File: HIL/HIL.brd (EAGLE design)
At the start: 129.5 x 103.9 mm, 269 parts, among them J1 JTAG_ARM_10PIN, J4 JTAG_ARM_10PIN, M0S0 TPB1,27, M0S1 TPB1,27, M0S2 TPB1,27, M0S3 TPB1,27, M1S0 M0S3, M1S1 M0S3, M1S2 M0S3, M1S3 M0S3, M2S0 M0S3, M2S1 M0S3, M2S2 M0S3, M2S3 M0S3, U1 CD74HC4067SM96, U10 INA219AIDCNR, U11 INA219AIDCNR, U12 INA219AIDCNR, U13 TM4C1294NCPDT, U14 ADUM1201ARZ, U15 SN65HVD230D, U16 TL1963AKTTR., U17 FT230XS, U2 TL1963AKTTR., U3 CD74HC4067SM96, U4 CD74HC4067SM96, U5 MCP4725A0T-E/CH, U6 TL1963AKTTR., U7 MCP2003-E/SN, U9 INA219AIDCNR, X1 A1944-50, X2 A1944-50, X4 A1944-50, Y3 NX3225GA

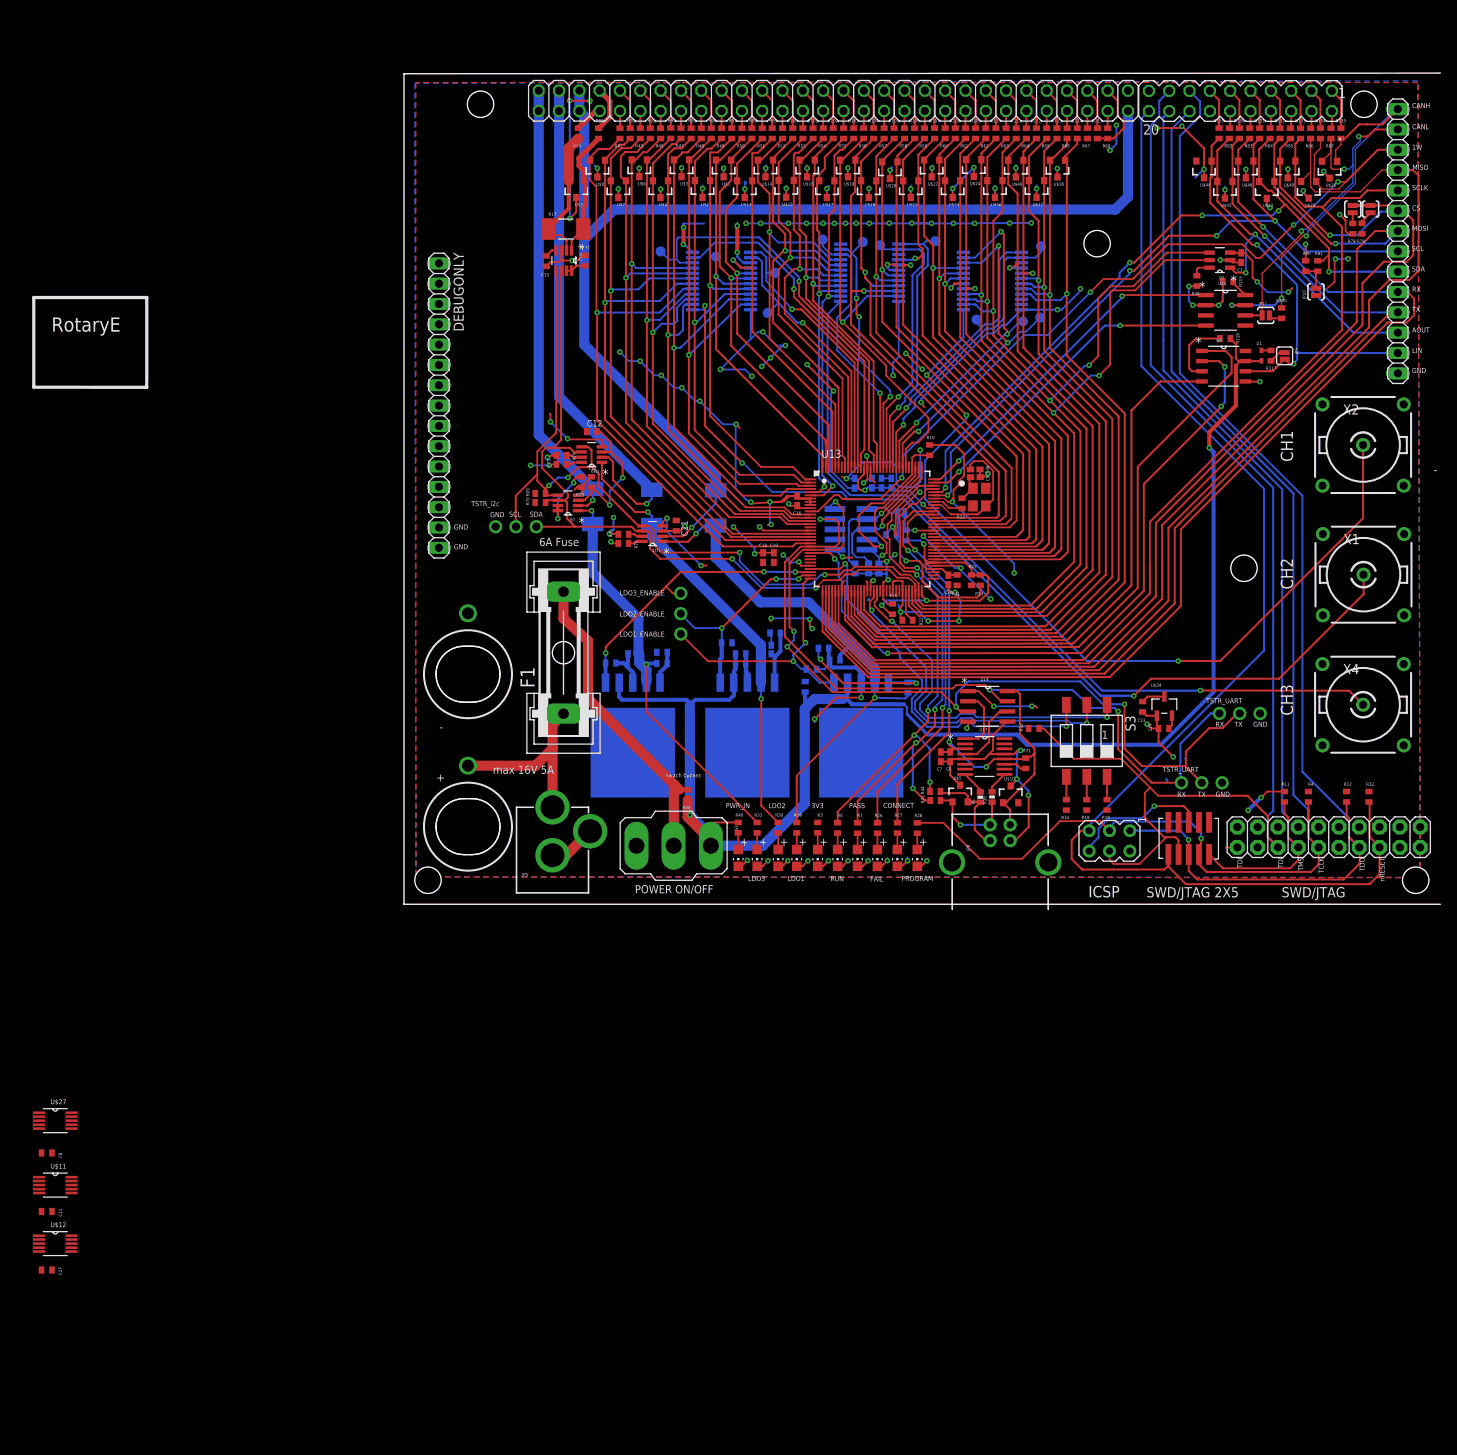
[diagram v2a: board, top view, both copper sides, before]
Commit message: Remove: 1 chanel DAC Add: 8 CH DAC Update: libraries
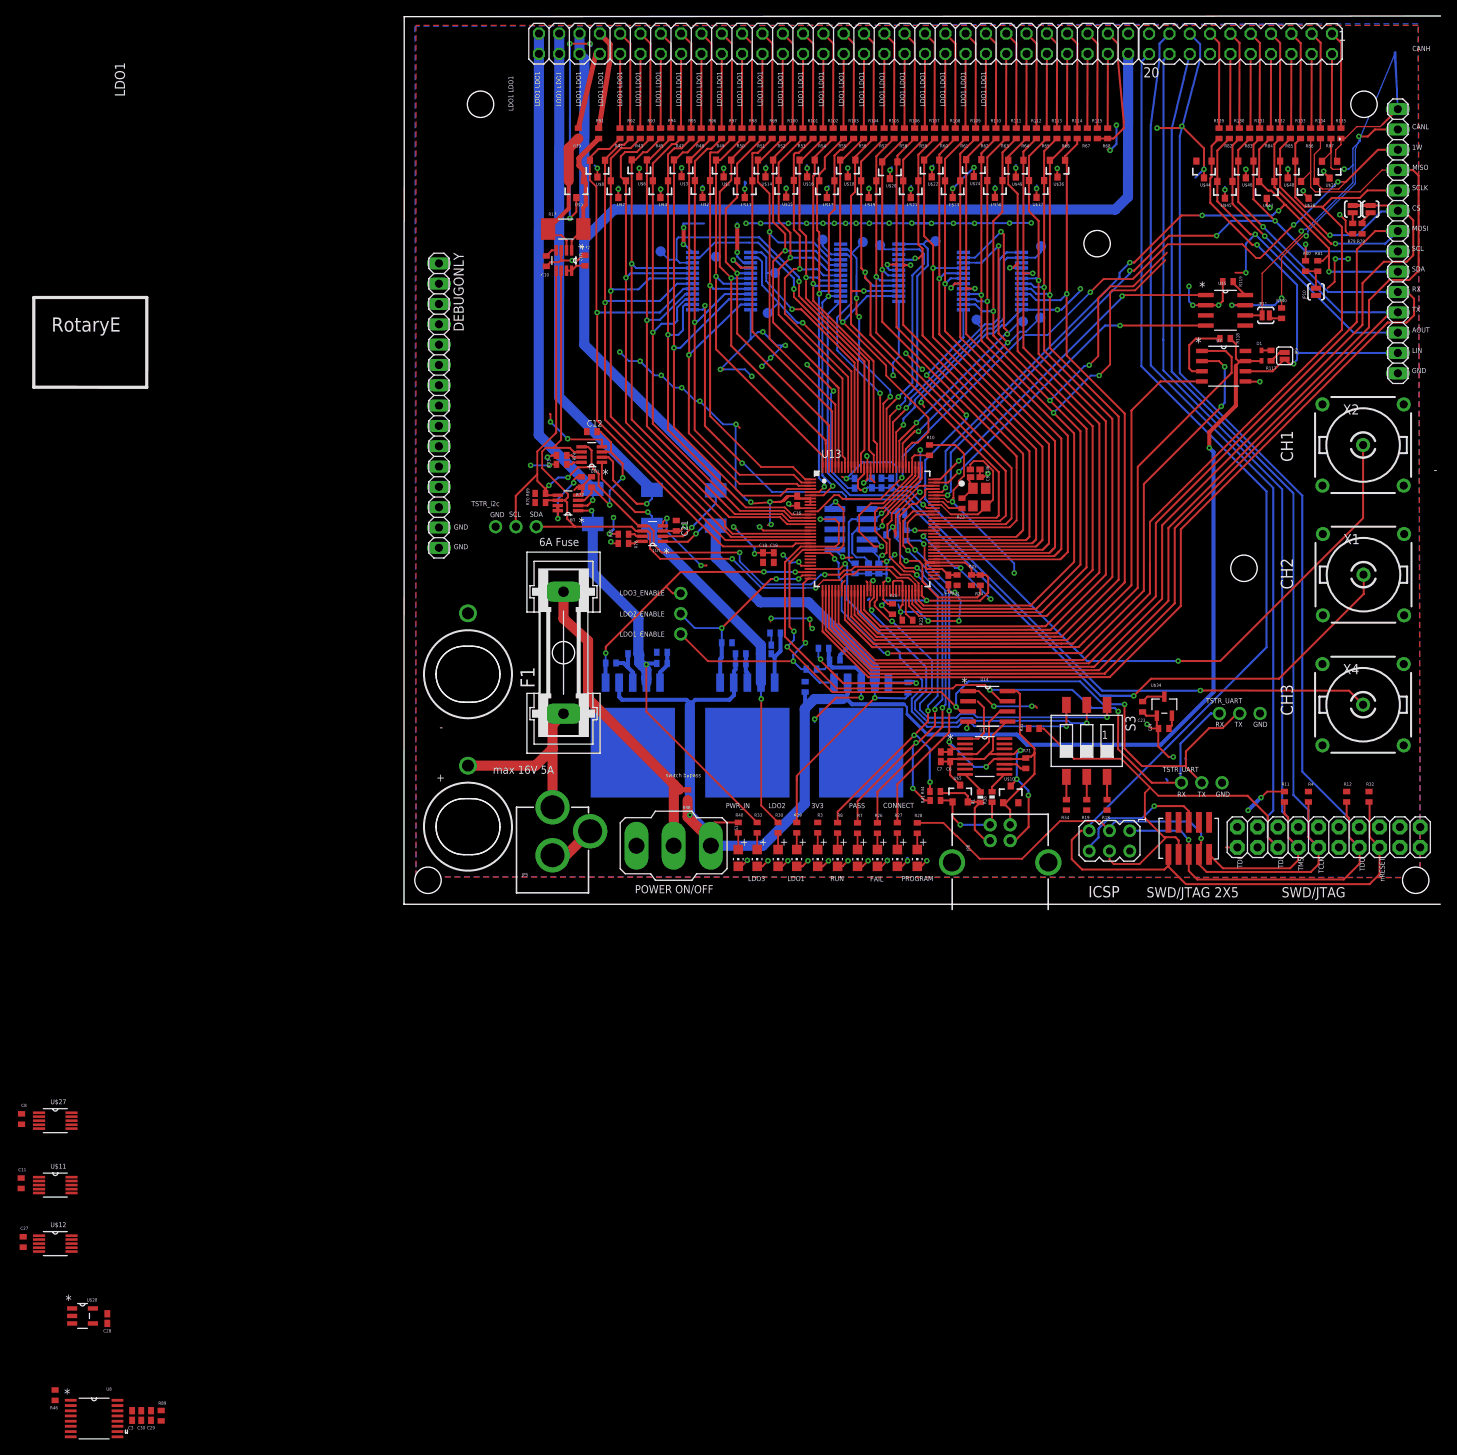
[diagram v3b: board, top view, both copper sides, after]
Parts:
- removed U5: MCP4725A0T-E/CH, MCP4725:SOT95P270X145-6N
- added C28: 0.1uF, rcl:C0402K
- added C29: 1uF, rcl:C0402K
- added C30: 10uF, rcl:C0402K
- added R89: 4k7, resistor:R0402
- added U$28: 24AA04T-I/OT, microchip_E14:SOT95P290X145-5N
- added U8: DAC7578SPW, Texas Instruments_E14:SOP65P640X120-16N
- R46: value 4.7k -> 4k7
- moved C3 200.4 mm to (-34.0, -63.9)
- moved R46 199.4 mm to (-43.6, -61.4)
- moved JP6 7.14 mm to (55.0, 107.6)
- moved SV1 7.14 mm to (104.6, 107.5)
- moved C8 5.28 mm to (-47.8, -26.8), turned to 90 degrees
- moved C11 4.77 mm to (-47.9, -34.9), turned to 90 degrees
- moved C27 4.58 mm to (-47.6, -42.2), turned to 90 degrees
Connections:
- net ADJ3 renamed LDO1_ADJ
- net ADJ4 renamed LDO2_ADJ
- net ADJ5 renamed LDO3_ADJ
- net N$40 renamed VIN
- removed net N$216: C23.1, U$34.3
- new net AOUT_1: U8.4
- new net AOUT_2: U8.13
- new net AOUT_3: U8.5
- new net AOUT_4: U8.12
- new net AOUT_5: U8.6
- new net AOUT_6: U8.11
- new net AOUT_7: U8.7
- new net AOUT_8: U8.10
- new net N$40: C29.2, C3.2, C30.2, R46.1, R89.2, U8.3, U8.8
- new net N$81: R89.1, U8.9
- net DUT_AOUT1: no longer U5.1
- net GND: now also C28.1, C29.1, C3.1, C30.1, U$28.2, U$28.5, U8.14; no longer C3.2, R46.2, U5.2
- net HOST_UART_TX: now also U14.7; no longer U14.2
- net N$1: now also R46.2, U8.1; no longer R46.1, U5.6
- net POWER_IN_12V: now also C23.1, U$34.3
- net TSTR_3V3: now also C28.2, U$28.4; no longer C3.1, U5.3
- net TSTR_RX: now also U14.2; no longer U14.7
- net TSTR_SCL: now also U$28.1, U8.16; no longer U5.5
- net TSTR_SDA: now also U$28.3, U8.15; no longer U5.4
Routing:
- net DUT_CAN_P: track 52.6 -> 72.2 mm
- net LDO1: track 147.9 -> 162.2 mm
- net TSTR_3V3: track 321.4 -> 310.1 mm, vias 71 -> 69
- net GND: track 319.1 -> 329.5 mm, vias 84 -> 83
- net NRESET: track 162.5 -> 169.9 mm
- net N$62: track 2.16 -> 9.30 mm
- net N$61: track 2.16 -> 9.30 mm
- net N$59: track 2.16 -> 9.30 mm
- net N$4: track 2.16 -> 9.30 mm
- net N$60: track 2.16 -> 9.30 mm
- net N$58: track 2.16 -> 9.30 mm
- net N$26: track 2.17 -> 9.30 mm
- net N$21: track 2.15 -> 9.29 mm
- net N$9: track 2.14 -> 9.28 mm
- net N$39: track 2.14 -> 9.28 mm
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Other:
- board size 129.5 x 103.9 mm -> 129.6 x 111 mm
- board text added: "LDO1 LDO1"
